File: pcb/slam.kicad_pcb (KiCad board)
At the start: 4 copper layers, 40.7 x 40.9 mm, 64 parts, among them J1 Conn_01x02_Pin, J10 Conn_01x06_Socket, J11 Conn_01x08_Pin, J2 Conn_02x02_Odd_Even, J3 USB_C_Receptacle_USB2.0_16P, J4 Conn_01x02_Pin, J5 Conn_01x02_Pin, J6 Conn_01x02_Pin, J7 Conn_01x02_Pin, J8 Conn_01x02_Pin, J9 Conn_01x04_Socket, Q1 AO3400A, SW1 SW_Push, SW2 SW_Push, U1 STM32F401RETx, U2 TLV1117-33, U3 DRV8833PWP, U4 DRV8833PWP, U5 HYCW110-TF10-180B, Y1 25 MHz

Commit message: cleanup pcb
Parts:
- moved R8 2.71 mm to (89.8, 103.4), turned to 90 degrees
- moved R7 1.32 mm to (87.8, 103.4), turned to -90 degrees
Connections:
- R8 pad 1: TIM1_CH1 -> Net-(Q1-G)
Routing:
- net +5V: track 21.1 -> 18.3 mm
- net Net-(Q1-G): track 2.63 -> 5.06 mm
- net /Motors/LIDAR_OUT2: track 7.40 -> 5.33 mm
- net GND: track 99.8 -> 101.0 mm
- net TIM1_CH1: track 7.59 -> 6.44 mm
- net SD_D1: track 16.5 -> 16.0 mm
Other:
- board text added: "1"
- board text added: "2"
- board text added: "3"
- board text added: "4"
- board text added: "@grimsteel"
- board text added: "JLCJLCJLCJLC"
- board text added: "git:${GIT_HASH}"

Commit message: pcb update
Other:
- board text added: "git:f8238f4"
- board text removed: "git:${GIT_HASH}"

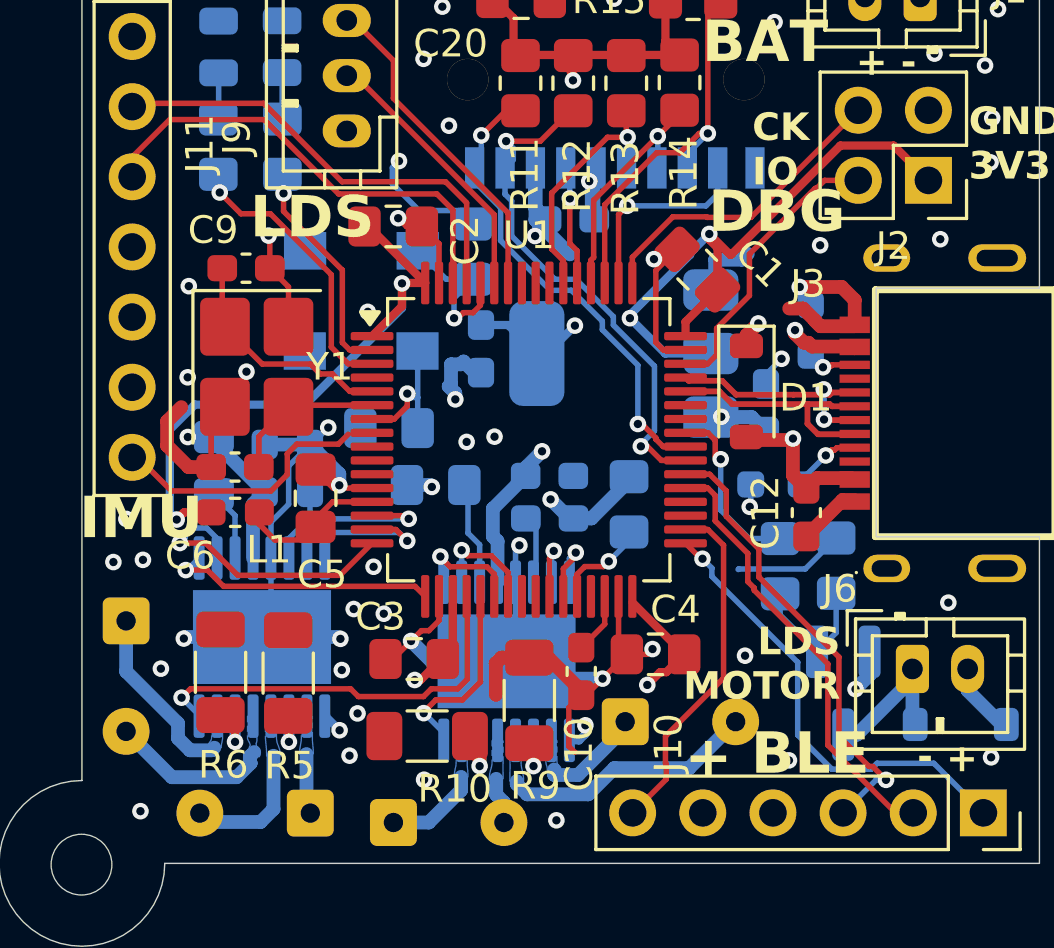
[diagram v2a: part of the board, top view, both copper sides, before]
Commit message: pcb: fix boot button and some traces
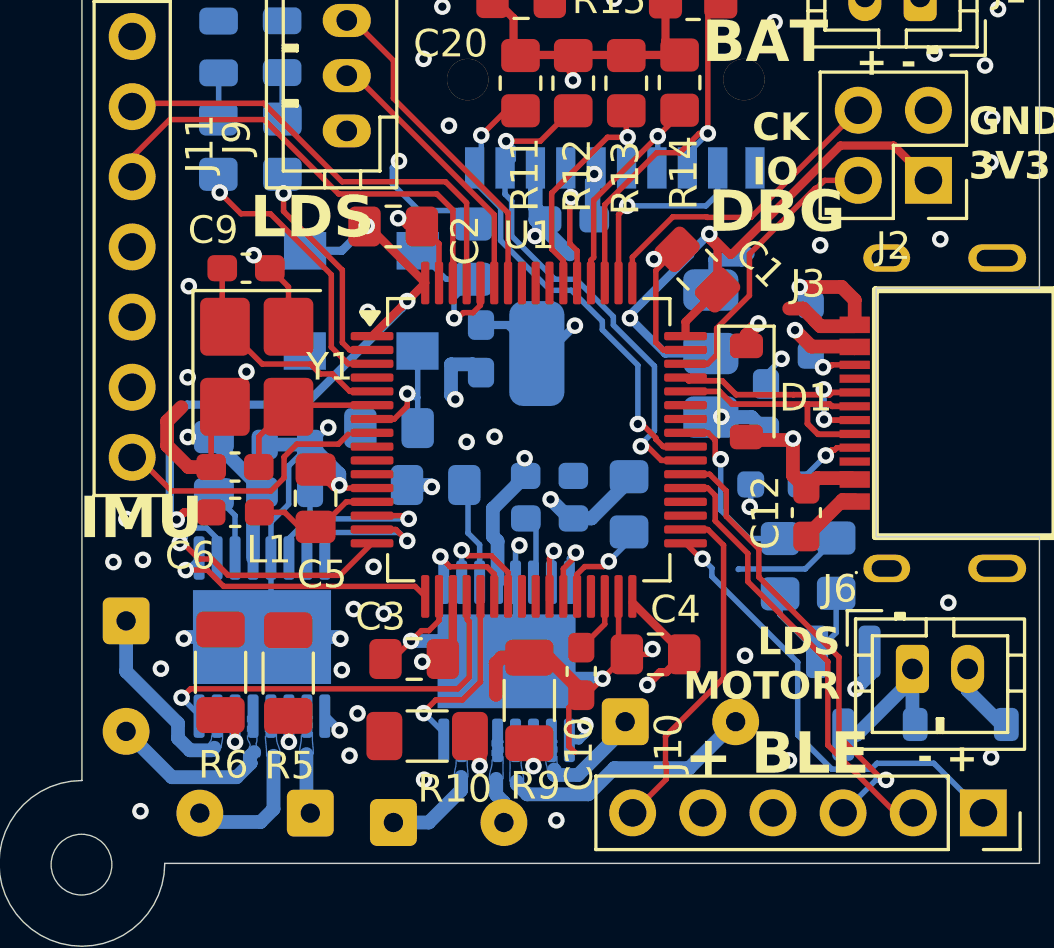
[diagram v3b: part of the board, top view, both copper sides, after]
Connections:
- SW1 pad 1: +3.3V -> +3V3
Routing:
- net +3V3: track 115.1 -> 117.3 mm, vias 11 -> 12
- net +5V: track 18.3 -> 19.0 mm
